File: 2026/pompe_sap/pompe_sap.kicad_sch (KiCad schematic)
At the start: 21 parts, among them J1 Conn_01x02_Pin, J2 22-03-5035, Q1 IRLML6344 (modèle du 6244), Q2 IRLML6344 (modèle du 6244), U2 NCP718xSN120, U3 INA180A1, U4 STM32L432KCUx

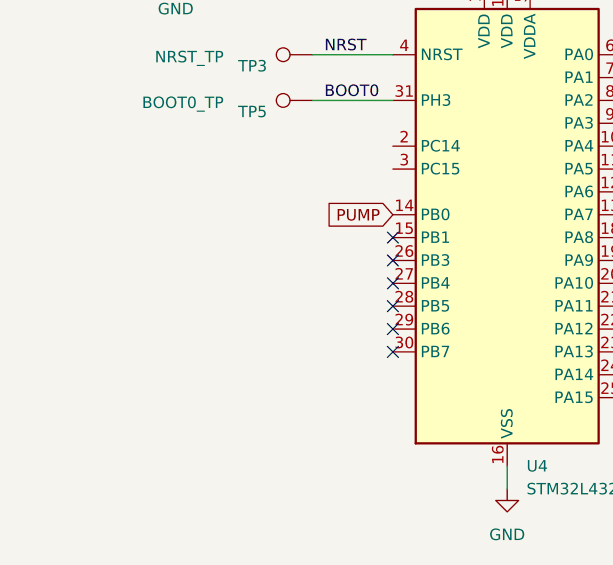
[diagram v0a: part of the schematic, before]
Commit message: [pompe SAP] Ajoute UART debug test points and LED.
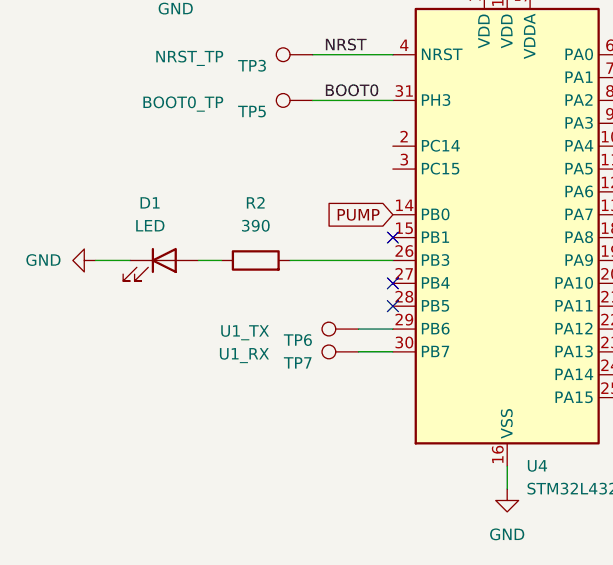
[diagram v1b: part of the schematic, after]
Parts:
- added D1: LED, LED_SMD:LED_0603_1608Metric, symbol Device:LED
- added R2: 390, Resistor_SMD:R_0603_1608Metric, symbol Device:R
- added TP6: U1_TX, TestPoint:TestPoint_Pad_D1.0mm, symbol Connector:TestPoint
- added TP7: U1_RX, TestPoint:TestPoint_Pad_D1.0mm, symbol Connector:TestPoint
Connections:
- net GND: now also D1.1 (K)
- net at U4.26 (PB3): now also R2.2
- net at U4.29 (PB6): now also TP6.1
- net at U4.30 (PB7): now also TP7.1
- new net: D1.2 (A), R2.1
- no-connect marks 17 -> 14
